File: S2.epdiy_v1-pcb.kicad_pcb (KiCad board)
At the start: 4 copper layers, 106.6 x 58.9 mm, 93 parts, among them J1 USB_C_Receptacle_USB2.0, J2 Jack-DC, P1 CONN_02X13, Q1 MMBT3904, Q2 MMBT3904, SW1 RESET, SW2 BOOT, U1 MCP1700-3302E_SOT23, U11 TP4056, U2 ESP32-S2-WROVER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

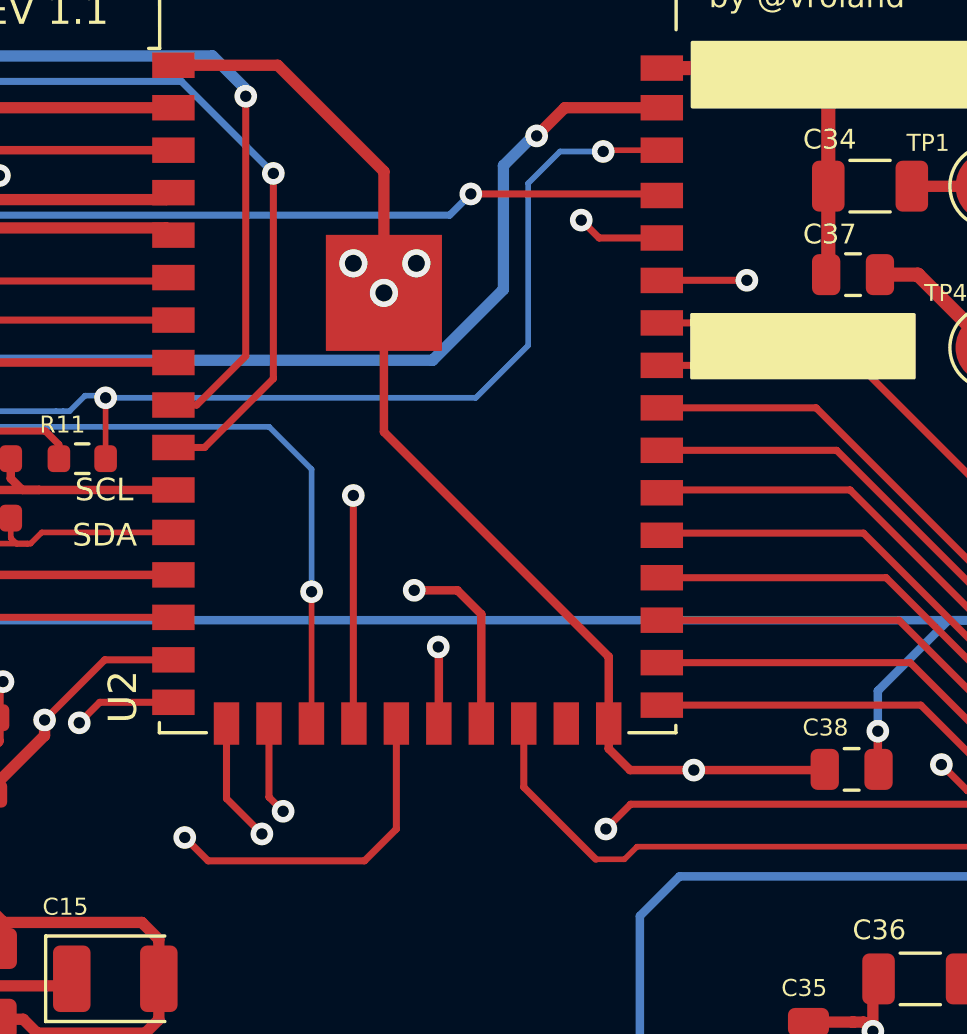
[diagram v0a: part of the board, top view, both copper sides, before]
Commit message: Modify IO config and use Realtime ones for I2S
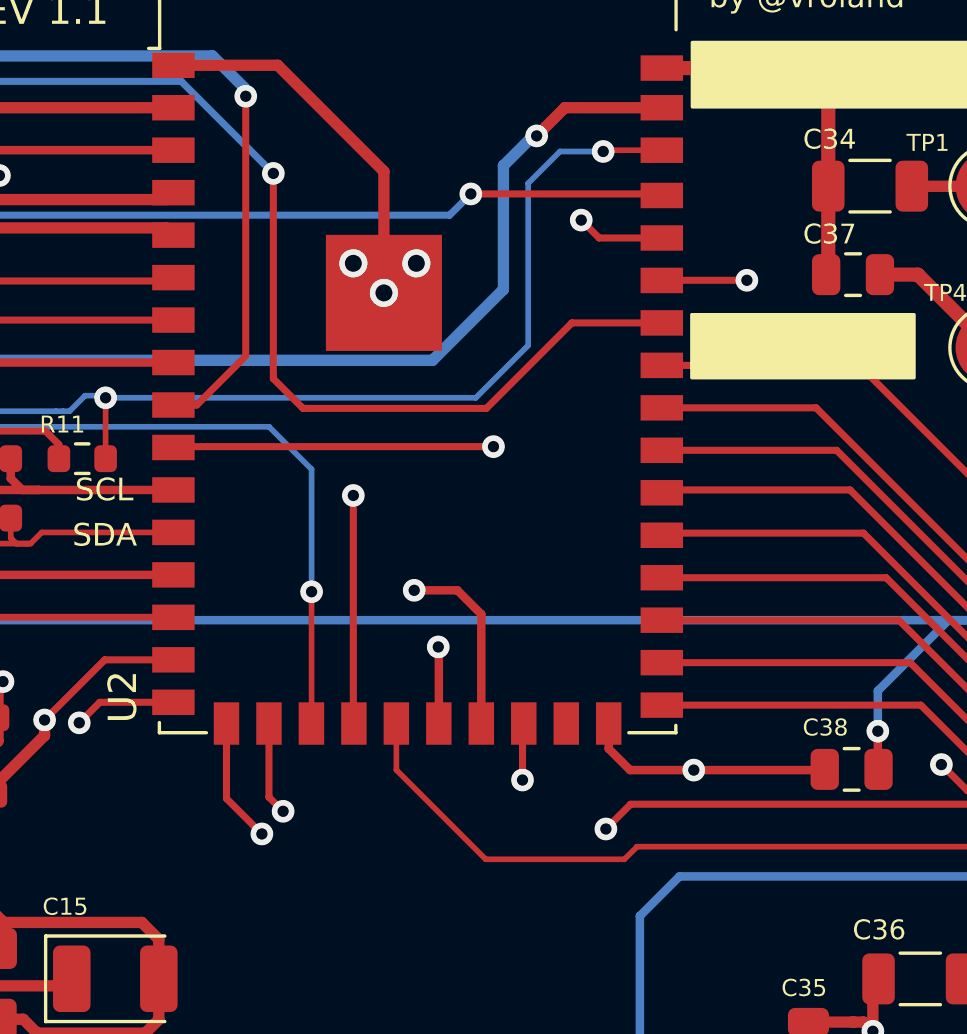
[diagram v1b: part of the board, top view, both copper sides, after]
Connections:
- P1 pad 7: /IO07 -> /IO42
- U2 pad 10: /IO07 -> /EP_STH
- U2 pad 21: /TPS_WAKEUP -> /EP_CKH
- U2 pad 24: /EP_CKH -> /TPS_WAKEUP
- U2 pad 36: /EP_STH -> /IO42
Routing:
- net /IO42: track 0.00 -> 65.6 mm, vias 0 -> 2
- net /IO07: track 54.7 -> 0.00 mm, vias 2 -> 0
- net GND: track 283.9 -> 265.4 mm
- net /EP_STH: track 30.1 -> 45.1 mm
- net /EP_CKH: track 26.0 -> 30.2 mm
- net /TPS_WAKEUP: track 33.1 -> 36.4 mm

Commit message: Correct silk
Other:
- board text added: "IO42"
- board text removed: "IO07"
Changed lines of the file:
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@@
     (effects (font (size 0.8 0.8) (thickness 0.15)))
   )
-  (gr_text "IO07" (at 126.179 73.58 90) (layer "F.SilkS")
+  (gr_text "IO42" (at 126.179 73.58 90) (layer "F.SilkS")
     (effects (font (size 0.8 0.8) (thickness 0.15)))
   )
